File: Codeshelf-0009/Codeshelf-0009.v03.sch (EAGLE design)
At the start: 26 parts, among them J1 CONTACT-SPRING-S7071-42R, J2 CONTACT-SPRING-S7071-42R, J3 CONTACT-SPRING-S7071-42R, J4 CONTACT-SPRING-S7071-42R, U1 MC9S08QG-DT, U2 LED5060A, U3 RS485SOIC, U4 CAT9552

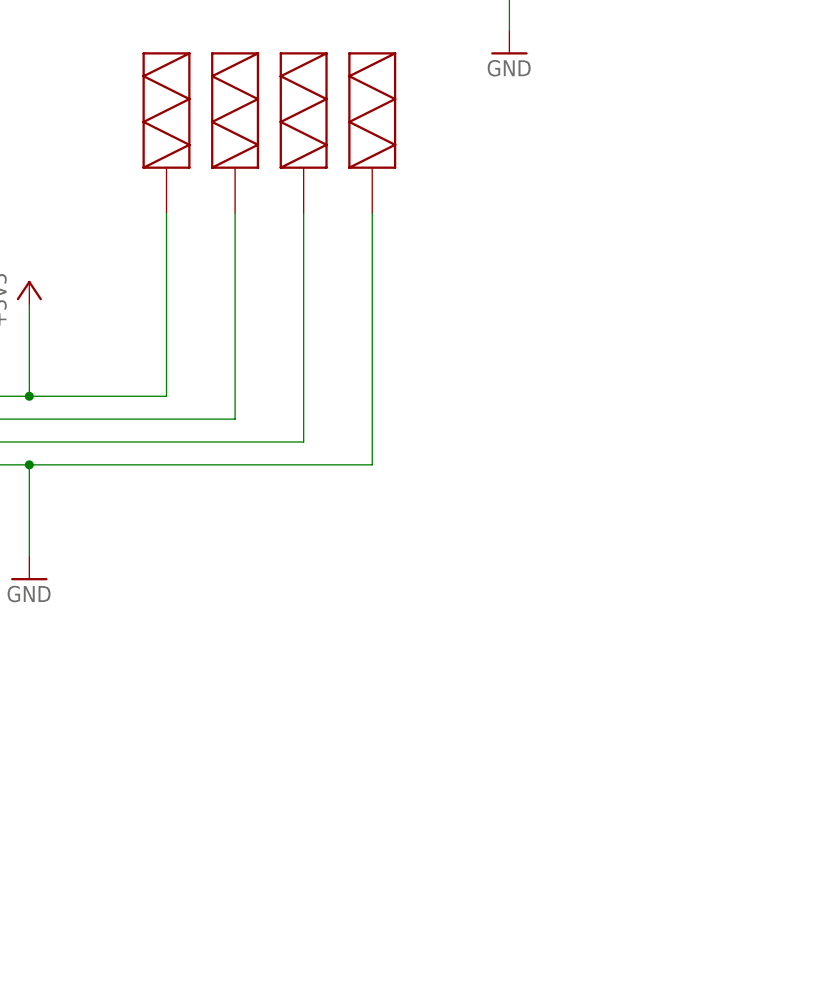
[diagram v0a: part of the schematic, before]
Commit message: KW2 and Slotflex edits
Removed RTC crystal from KW2, fixed (connected) switches in schematic of
0009.v02 and Slotflex v3 with RJ45 with NEW pinout (compatible with new
scanner pinout which doesn't exist yet in a CHE).
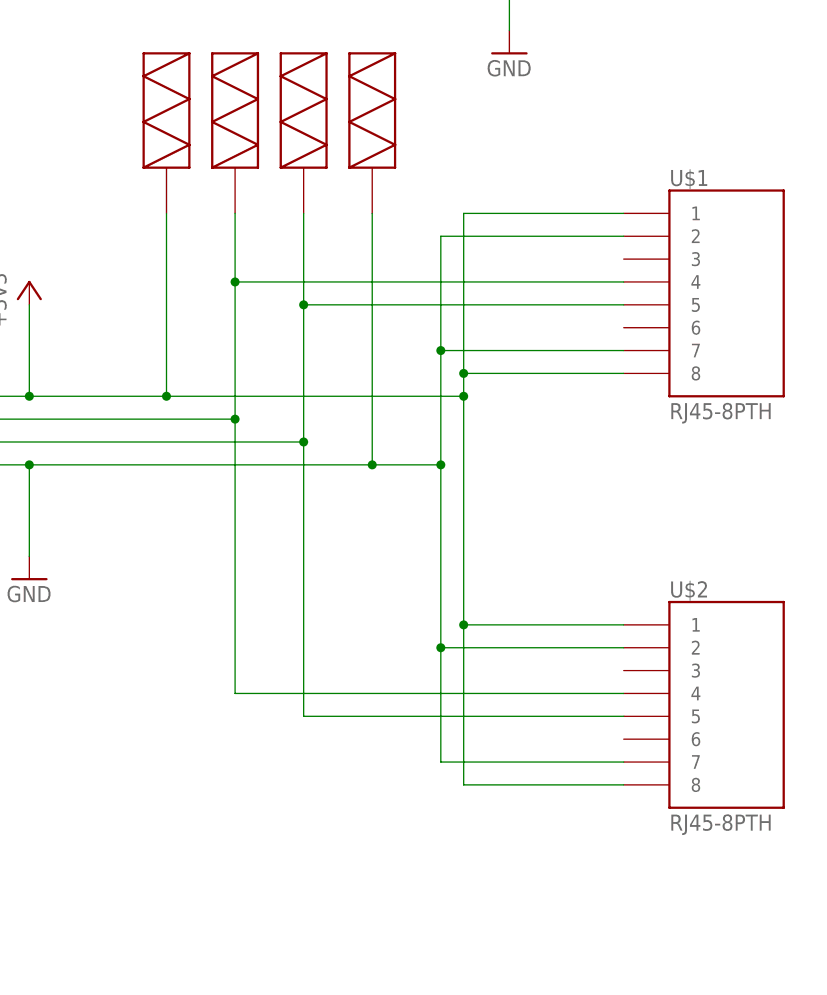
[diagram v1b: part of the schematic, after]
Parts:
- added U$1, U$2: RJ45-8PTH, GW-devices:RJ45-8PTH
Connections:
- net +3V3: now also U$1.1, U$1.8, U$2.1, U$2.8
- net A: now also U$1.5, U$2.5
- net B: now also U$1.4, U$2.4
- net GND: now also U$1.2, U$1.7, U$2.2, U$2.7
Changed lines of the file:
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@@
 <attribute name="PRICE" value="0.18"/>
 </part>
+<part name="U$1" library="GW-devices" deviceset="RJ45-8" device="PTH"/>
+<part name="U$2" library="GW-devices" deviceset="RJ45-8" device="PTH"/>
 </parts>
 <sheets>
@@
 <attribute name="PRICE" x="124.46" y="58.42" size="6.4516" layer="96" display="off"/>
 </instance>
+<instance part="U$1" gate="G$1" x="170.18" y="-20.32"/>
+<instance part="U$2" gate="G$1" x="170.18" y="-66.04"/>
 </instances>
 <busses>
@@
 <pinref part="U3" gate="G$1" pin="GND"/>
 <pinref part="J4" gate="G$1" pin="P1"/>
+<wire x1="129.54" y1="-38.1" x2="137.16" y2="-38.1" width="0.1524" layer="91"/>
+<wire x1="137.16" y1="-38.1" x2="137.16" y2="-25.4" width="0.1524" layer="91"/>
+<junction x="129.54" y="-38.1"/>
+<pinref part="U$1" gate="G$1" pin="2"/>
+<wire x1="137.16" y1="-25.4" x2="137.16" y2="-12.7" width="0.1524" layer="91"/>
+<wire x1="157.48" y1="-12.7" x2="137.16" y2="-12.7" width="0.1524" layer="91"/>
+<pinref part="U$1" gate="G$1" pin="7"/>
+<wire x1="157.48" y1="-25.4" x2="137.16" y2="-25.4" width="0.1524" layer="91"/>
+<junction x="137.16" y="-25.4"/>
+<wire x1="137.16" y1="-38.1" x2="137.16" y2="-58.42" width="0.1524" layer="91"/>
+<junction x="137.16" y="-38.1"/>
+<pinref part="U$2" gate="G$1" pin="2"/>
+<wire x1="137.16" y1="-58.42" x2="157.48" y2="-58.42" width="0.1524" layer="91"/>
+<wire x1="137.16" y1="-58.42" x2="137.16" y2="-71.12" width="0.1524" layer="91"/>
+<junction x="137.16" y="-58.42"/>
+<pinref part="U$2" gate="G$1" pin="7"/>
+<wire x1="137.16" y1="-71.12" x2="157.48" y2="-71.12" width="0.1524" layer="91"/>
 </segment>
 <segment>
@@
 <pinref part="U3" gate="G$1" pin="VCC"/>
 <pinref part="J1" gate="G$1" pin="P1"/>
+<pinref part="U$1" gate="G$1" pin="1"/>
+<wire x1="157.48" y1="-10.16" x2="139.7" y2="-10.16" width="0.1524" layer="91"/>
+<wire x1="139.7" y1="-10.16" x2="139.7" y2="-27.94" width="0.1524" layer="91"/>
+<wire x1="139.7" y1="-27.94" x2="139.7" y2="-30.48" width="0.1524" layer="91"/>
+<wire x1="139.7" y1="-30.48" x2="106.68" y2="-30.48" width="0.1524" layer="91"/>
+<junction x="106.68" y="-30.48"/>
+<pinref part="U$1" gate="G$1" pin="8"/>
+<wire x1="157.48" y1="-27.94" x2="139.7" y2="-27.94" width="0.1524" layer="91"/>
+<junction x="139.7" y="-27.94"/>
+<wire x1="139.7" y1="-30.48" x2="139.7" y2="-55.88" width="0.1524" layer="91"/>
+<junction x="139.7" y="-30.48"/>
+<pinref part="U$2" gate="G$1" pin="1"/>
+<wire x1="139.7" y1="-55.88" x2="157.48" y2="-55.88" width="0.1524" layer="91"/>
+<wire x1="139.7" y1="-55.88" x2="139.7" y2="-73.66" width="0.1524" layer="91"/>
+<junction x="139.7" y="-55.88"/>
+<pinref part="U$2" gate="G$1" pin="8"/>
+<wire x1="157.48" y1="-73.66" x2="139.7" y2="-73.66" width="0.1524" layer="91"/>
 </segment>
 <segment>
@@
 <segment>
 <wire x1="83.82" y1="-33.02" x2="114.3" y2="-33.02" width="0.1524" layer="91"/>
-<wire x1="114.3" y1="-33.02" x2="114.3" y2="-10.16" width="0.1524" layer="91"/>
+<wire x1="114.3" y1="-33.02" x2="114.3" y2="-17.78" width="0.1524" layer="91"/>
 <pinref part="U3" gate="G$1" pin="B"/>
 <pinref part="J2" gate="G$1" pin="P1"/>
+<pinref part="U$2" gate="G$1" pin="4"/>
+<wire x1="114.3" y1="-17.78" x2="114.3" y2="-10.16" width="0.1524" layer="91"/>
+<wire x1="157.48" y1="-63.5" x2="114.3" y2="-63.5" width="0.1524" layer="91"/>
+<wire x1="114.3" y1="-63.5" x2="114.3" y2="-33.02" width="0.1524" layer="91"/>
+<junction x="114.3" y="-33.02"/>
+<pinref part="U$1" gate="G$1" pin="4"/>
+<wire x1="157.48" y1="-17.78" x2="114.3" y2="-17.78" width="0.1524" layer="91"/>
+<junction x="114.3" y="-17.78"/>
 </segment>
 </net>
@@
 <segment>
 <wire x1="83.82" y1="-35.56" x2="121.92" y2="-35.56" width="0.1524" layer="91"/>
-<wire x1="121.92" y1="-35.56" x2="121.92" y2="-10.16" width="0.1524" layer="91"/>
+<wire x1="121.92" y1="-35.56" x2="121.92" y2="-20.32" width="0.1524" layer="91"/>
 <pinref part="U3" gate="G$1" pin="A"/>
 <pinref part="J3" gate="G$1" pin="P1"/>
-</segment>
-</net>
+<wire x1="121.92" y1="-20.32" x2="121.92" y2="-10.16" width="0.1524" layer="91"/>
+<wire x1="121.92" y1="-35.56" x2="121.92" y2="-66.04" width="0.1524" layer="91"/>
+<junction x="121.92" y="-35.56"/>
+<pinref part="U$2" gate="G$1" pin="5"/>
+<wire x1="121.92" y1="-66.04" x2="157.48" y2="-66.04" width="0.1524" layer="91"/>
+<pinref part="U$1" gate="G$1" pin="5"/>
+<wire x1="121.92" y1="-20.32" x2="157.48" y2="-20.32" width="0.1524" layer="91"/>
+<junction x="121.92" y="-20.32"/>
+</segment>
+</net>

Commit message: Started new SlotFlex Layout
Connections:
- net A renamed 485_P
- net B renamed 485_N
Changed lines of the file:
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@@
 </segment>
 </net>
-<net name="B" class="0">
+<net name="485_N" class="0">
 <segment>
 <wire x1="83.82" y1="-33.02" x2="114.3" y2="-33.02" width="0.1524" layer="91"/>
@@
 </segment>
 </net>
-<net name="A" class="0">
+<net name="485_P" class="0">
 <segment>
 <wire x1="83.82" y1="-35.56" x2="121.92" y2="-35.56" width="0.1524" layer="91"/>

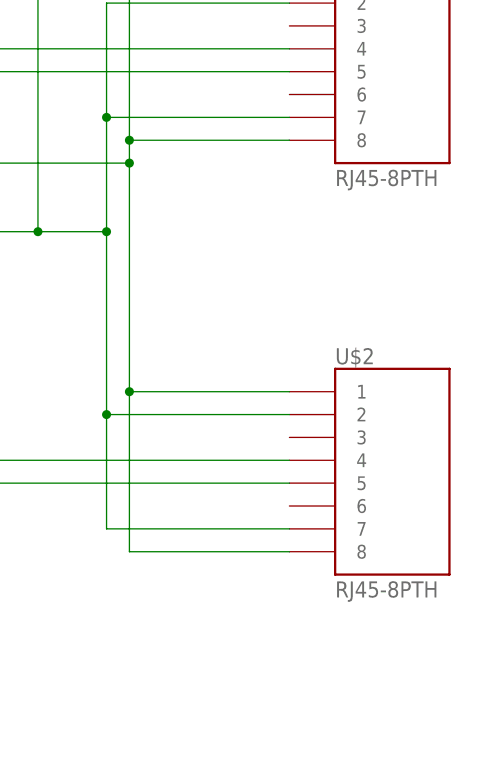
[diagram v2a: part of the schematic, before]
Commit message: Changed to SMD RJ45
Working on layout with new RJ45
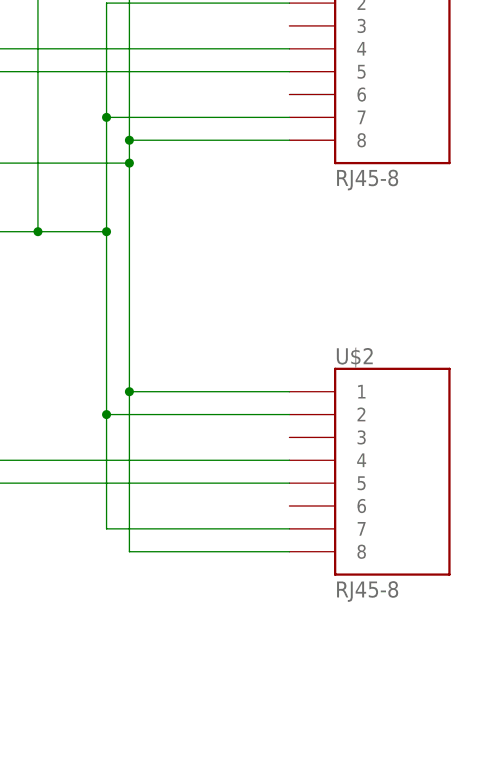
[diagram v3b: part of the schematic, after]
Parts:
- U$1, U$2: value RJ45-8PTH -> RJ45-8; device GW-devices:RJ45-8PTH -> GW-devices:RJ45-8
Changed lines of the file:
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@@
 <attribute name="PRICE" value="0.18"/>
 </part>
-<part name="U$1" library="GW-devices" deviceset="RJ45-8" device="PTH"/>
-<part name="U$2" library="GW-devices" deviceset="RJ45-8" device="PTH"/>
+<part name="U$1" library="GW-devices" deviceset="RJ45-8" device="" value="RJ45-8"/>
+<part name="U$2" library="GW-devices" deviceset="RJ45-8" device="" value="RJ45-8"/>
 </parts>
 <sheets>

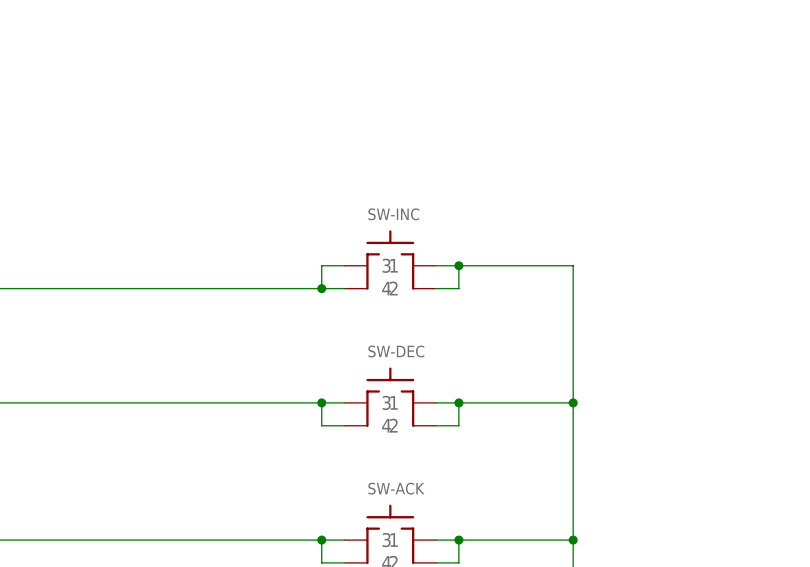
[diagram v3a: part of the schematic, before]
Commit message: Position controller CAD models
Worked on exporting CAD models from Eagle for Marc. Chose form factor
for current version of small position controllers (NEMA enclosure lid)
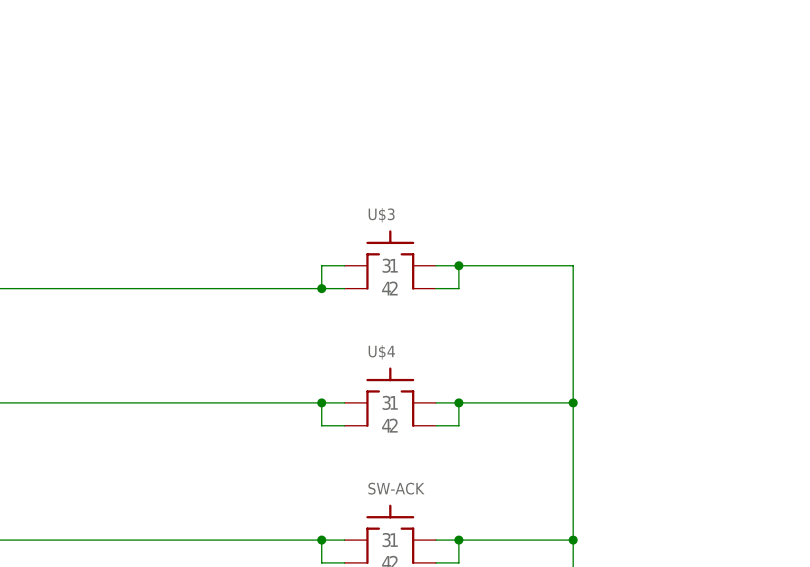
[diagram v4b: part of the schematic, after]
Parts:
- removed SW-DEC, SW-INC: SWITCH-TACTILE-FSM, GW-devices:SWITCH-TACTILE-FSM
- added U$3, U$4: SWITCH-TACTILE, GW-devices:SWITCH-TACTILE
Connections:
- net GND: now also U$3.3, U$3.4, U$4.3, U$4.4; no longer SW-DEC.3, SW-DEC.4, SW-INC.3, SW-INC.4
- net N$43: now also U$4.1, U$4.2; no longer SW-DEC.1, SW-DEC.2
- net N$45: now also U$3.1, U$3.2; no longer SW-INC.1, SW-INC.2
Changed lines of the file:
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@@
 <part name="GND5" library="supply1" deviceset="GND" device=""/>
 <part name="SW-ACK" library="GW-devices" deviceset="SWITCH-TACTILE" device="-320.03E11"/>
-<part name="SW-DEC" library="GW-devices" deviceset="SWITCH-TACTILE" device="-FSM">
-<attribute name="MFGN" value="TE Connectivity"/>
-<attribute name="MFGP" value="FSM16JH"/>
-<attribute name="PRICE" value="0.18"/>
-</part>
-<part name="SW-INC" library="GW-devices" deviceset="SWITCH-TACTILE" device="-FSM">
-<attribute name="MFGN" value="TE Connectivity"/>
-<attribute name="MFGP" value="FSM16JH"/>
-<attribute name="PRICE" value="0.18"/>
-</part>
 <part name="U$1" library="GW-devices" deviceset="RJ45-8" device="" value="RJ45-8"/>
 <part name="U$2" library="GW-devices" deviceset="RJ45-8" device="" value="RJ45-8"/>
+<part name="U$3" library="GW-devices" deviceset="SWITCH-TACTILE" device="" value="SWITCH-TACTILE"/>
+<part name="U$4" library="GW-devices" deviceset="SWITCH-TACTILE" device="" value="SWITCH-TACTILE"/>
 </parts>
 <sheets>
@@
 <instance part="GND5" gate="1" x="144.78" y="7.62"/>
 <instance part="SW-ACK" gate="G$1" x="124.46" y="27.94"/>
-<instance part="SW-DEC" gate="G$1" x="124.46" y="43.18">
-<attribute name="MFGN" x="124.46" y="43.18" size="6.4516" layer="96" display="off"/>
-<attribute name="MFGP" x="124.46" y="43.18" size="6.4516" layer="96" display="off"/>
-<attribute name="PRICE" x="124.46" y="43.18" size="6.4516" layer="96" display="off"/>
-</instance>
-<instance part="SW-INC" gate="G$1" x="124.46" y="58.42">
-<attribute name="MFGN" x="124.46" y="58.42" size="6.4516" layer="96" display="off"/>
-<attribute name="MFGP" x="124.46" y="58.42" size="6.4516" layer="96" display="off"/>
-<attribute name="PRICE" x="124.46" y="58.42" size="6.4516" layer="96" display="off"/>
-</instance>
 <instance part="U$1" gate="G$1" x="170.18" y="-20.32"/>
 <instance part="U$2" gate="G$1" x="170.18" y="-66.04"/>
+<instance part="U$3" gate="G$1" x="124.46" y="58.42"/>
+<instance part="U$4" gate="G$1" x="124.46" y="43.18"/>
 </instances>
 <busses>
@@
 <junction x="132.08" y="58.42"/>
 <pinref part="GND5" gate="1" pin="GND"/>
-<pinref part="SW-DEC" gate="G$1" pin="4"/>
 <pinref part="SW-ACK" gate="G$1" pin="4"/>
-<pinref part="SW-INC" gate="G$1" pin="4"/>
-<pinref part="SW-INC" gate="G$1" pin="3"/>
-<pinref part="SW-DEC" gate="G$1" pin="3"/>
 <pinref part="SW-ACK" gate="G$1" pin="3"/>
+<pinref part="U$3" gate="G$1" pin="3"/>
+<pinref part="U$3" gate="G$1" pin="4"/>
+<pinref part="U$4" gate="G$1" pin="3"/>
+<pinref part="U$4" gate="G$1" pin="4"/>
 </segment>
 </net>
@@
 <wire x1="116.84" y1="40.64" x2="119.38" y2="40.64" width="0.1524" layer="91"/>
 <junction x="116.84" y="43.18"/>
-<pinref part="SW-DEC" gate="G$1" pin="1"/>
-<pinref part="SW-DEC" gate="G$1" pin="2"/>
 <wire x1="116.84" y1="43.18" x2="45.72" y2="43.18" width="0.1524" layer="91"/>
 <wire x1="45.72" y1="43.18" x2="45.72" y2="12.7" width="0.1524" layer="91"/>
 <pinref part="U1" gate="G$1" pin="PTA1/KBIP1"/>
 <wire x1="45.72" y1="12.7" x2="25.4" y2="12.7" width="0.1524" layer="91"/>
+<pinref part="U$4" gate="G$1" pin="1"/>
+<pinref part="U$4" gate="G$1" pin="2"/>
 </segment>
 </net>
 <net name="N$45" class="0">
 <segment>
-<pinref part="SW-INC" gate="G$1" pin="2"/>
-<pinref part="SW-INC" gate="G$1" pin="1"/>
 <wire x1="116.84" y1="58.42" x2="119.38" y2="58.42" width="0.1524" layer="91"/>
 <wire x1="116.84" y1="58.42" x2="116.84" y2="55.88" width="0.1524" layer="91"/>
@@
 <pinref part="U1" gate="G$1" pin="PTA0/KBIP0"/>
 <wire x1="25.4" y1="55.88" x2="25.4" y2="17.78" width="0.1524" layer="91"/>
-</segment>
-</net>
+<pinref part="U$3" gate="G$1" pin="1"/>
+<pinref part="U$3" gate="G$1" pin="2"/>
+</segment>
+</net>

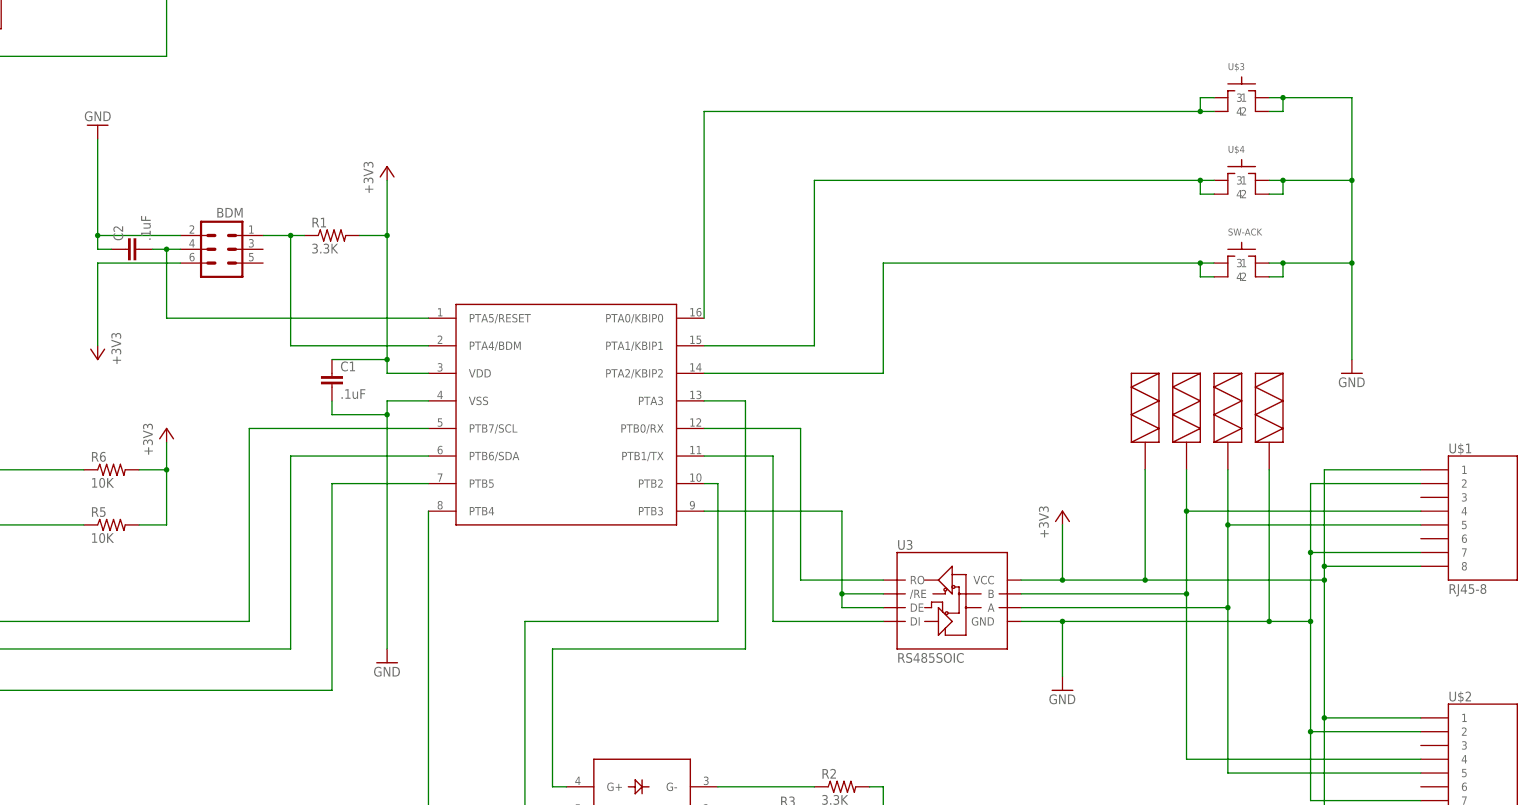
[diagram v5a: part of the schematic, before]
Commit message: New PosCon finished routing
Added RJ45 programming and awaiting new LED test.
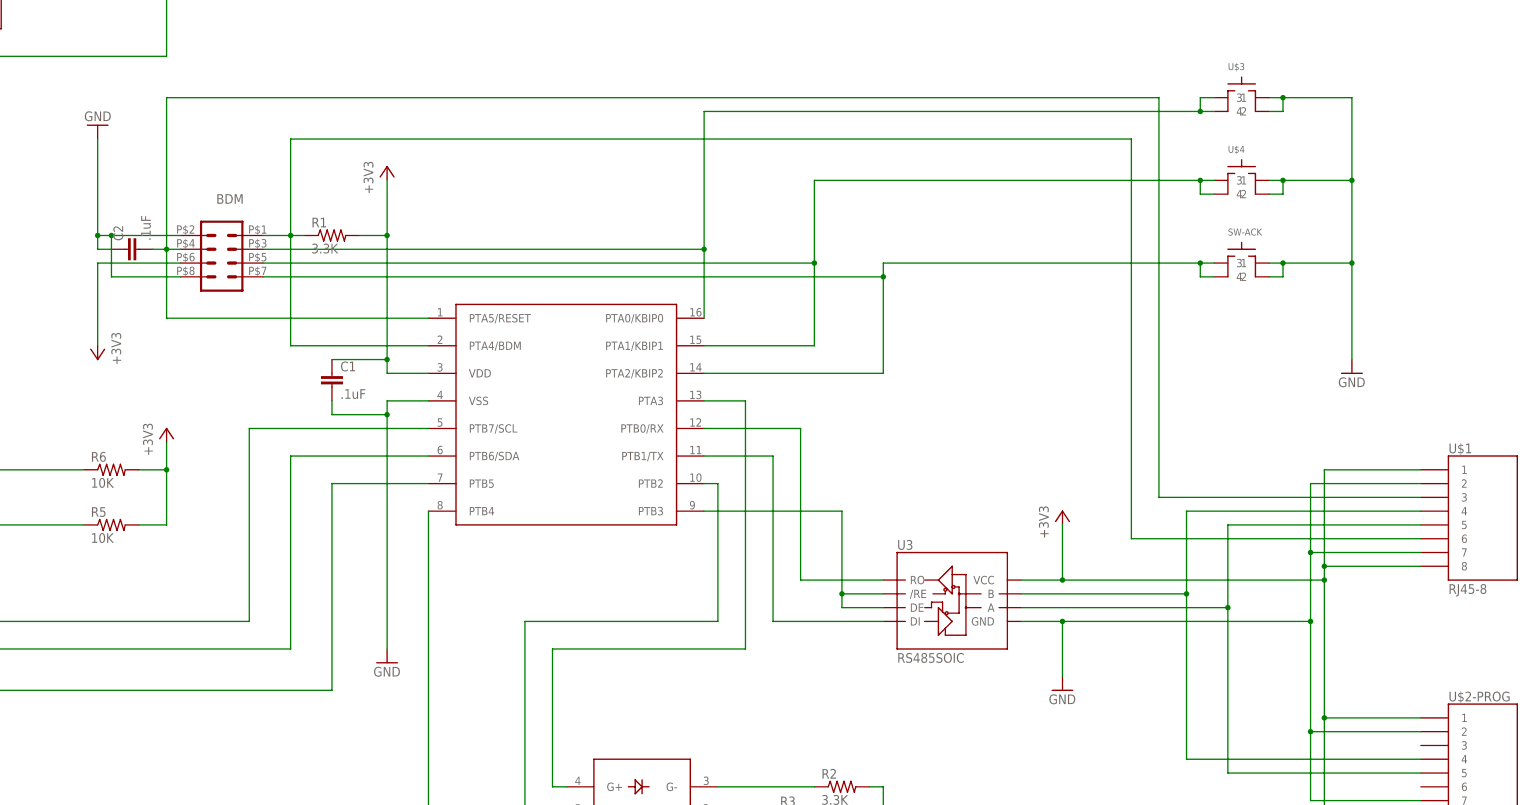
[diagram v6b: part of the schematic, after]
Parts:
- removed J1, J2, J3, J4: CONTACT-SPRING-S7071-42R, GW-devices:CONTACT-SPRING-S1761
- BDM: value HEADER-3X2 -> TP2X4SMD; device GW-devices:HEADER-3X2 -> GW-devices:TP2X4SMD
- renumbered U$2 to U$2-PROG
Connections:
- net +3V3: no longer J1.P1
- net 485_N: no longer J2.P1
- net 485_P: no longer J3.P1
- net GND: now also BDM.8; no longer J4.P1
- net N$23: now also U$1.3
- net N$42: now also BDM.7
- net N$43: now also BDM.5
- net N$45: now also BDM.3
- net N$9: now also U$1.6
